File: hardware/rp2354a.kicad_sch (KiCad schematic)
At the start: 31 parts, among them J2 SM03B-SRSS-TB, J3 AM32_1, J4 AM32_2, U4 RP2354A, Y1 ABM8-272-T3

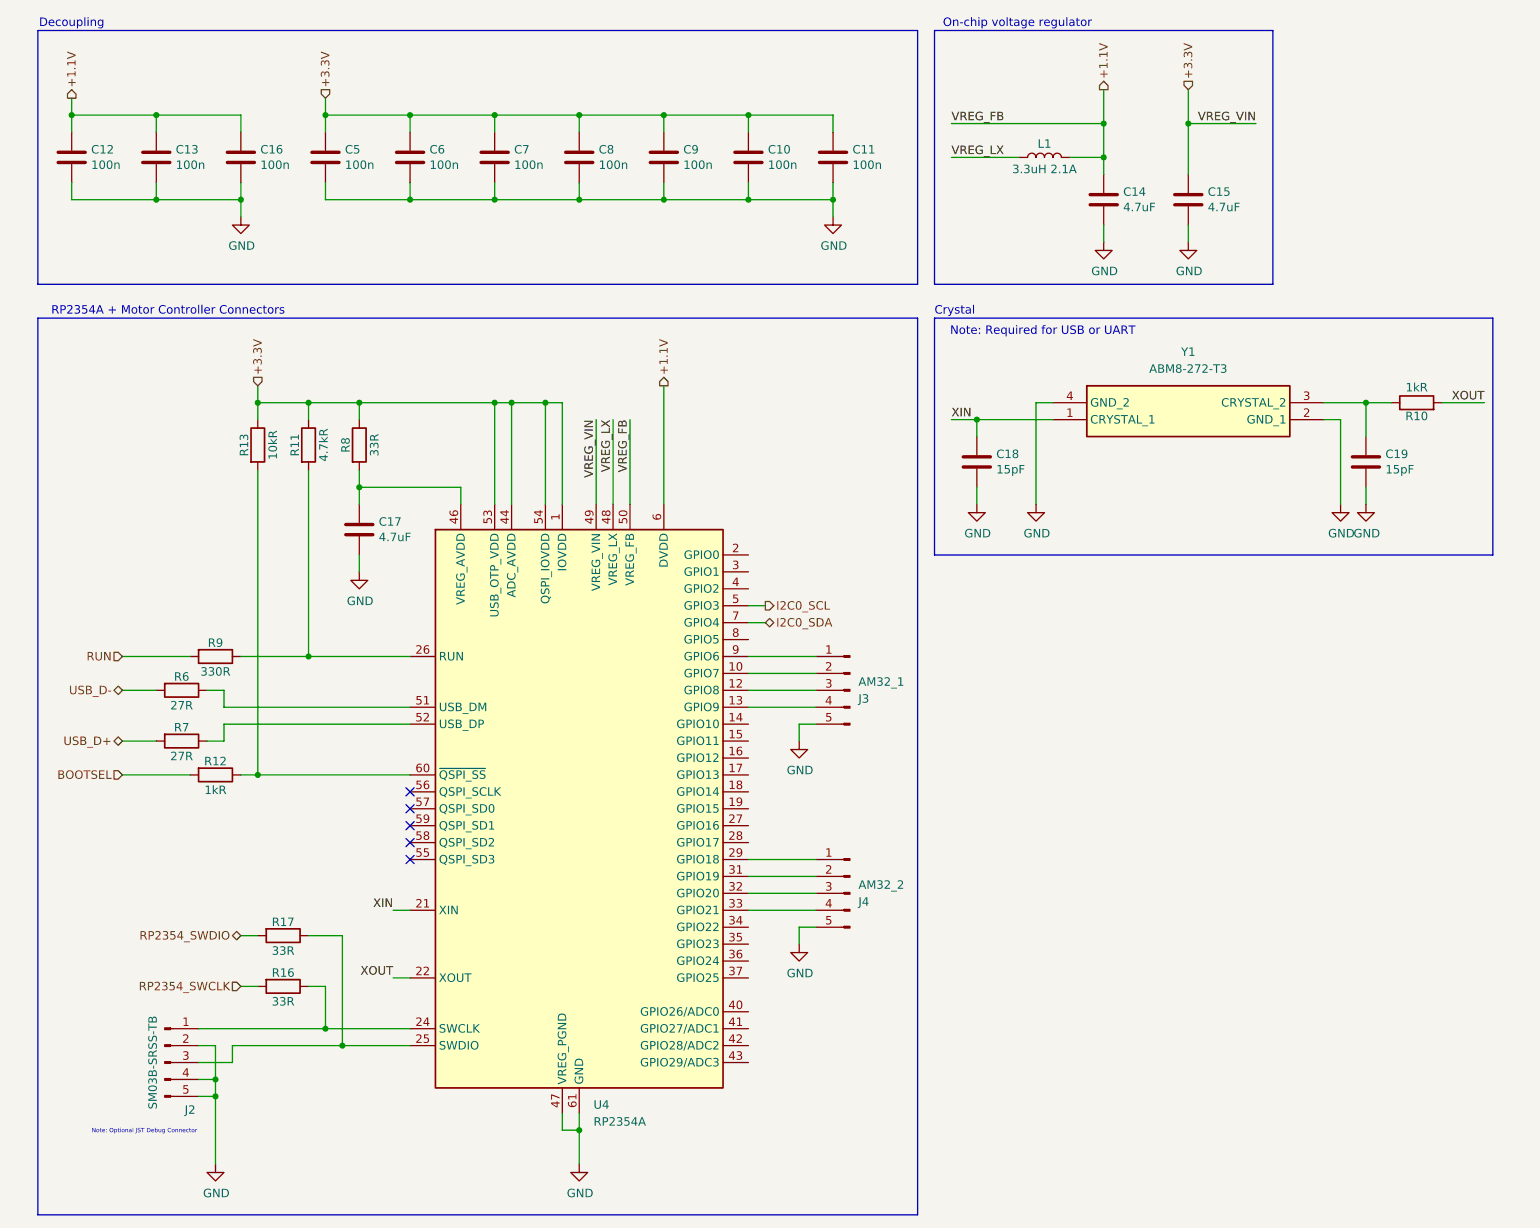
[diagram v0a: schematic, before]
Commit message: Add second camera, magnet load switch and schematic fixes
- Second camera J11 on MIPI1: I2C on ID_SD/ID_SC with 2.2k pull-ups,
  power enable on GPIO14/15 (CAM1_GPIO0/1); both cameras take 3.3 V
  from CM5_3.3V
- Magnet power switch: IC9 output is now +5V_AON, TPS22965 load switch
  IC15 drives +5V, J12 carries +5V_AON / MAG_ON / GND with R29
  pull-down; new TPS22965 symbol library
- Power: 4 A TPSM53604, 8 mOhm input sense resistor, C39/C40 bulk caps,
  F1-F3 battery polyfuses; 5 V raised to 5.115 V (R24 2.43k, 0.5 %
  feedback resistors); 47 uF at the CM5 5 V pins
- BMI270 on SPI and WSEN-PADS on I2C in serial_peripherals.kicad_sch
- Breakout headers J9/J13 with 5 V, 3.3 V and GND
- References renamed U -> IC; net classes for DPHY1, +5V, +5V_AON, +3.3V
- ERC clean (0 errors, 0 warnings); PCB update from the schematic is
  still in progress

Co-Authored-By: Claude Opus 5.5 <noreply@anthropic.com>
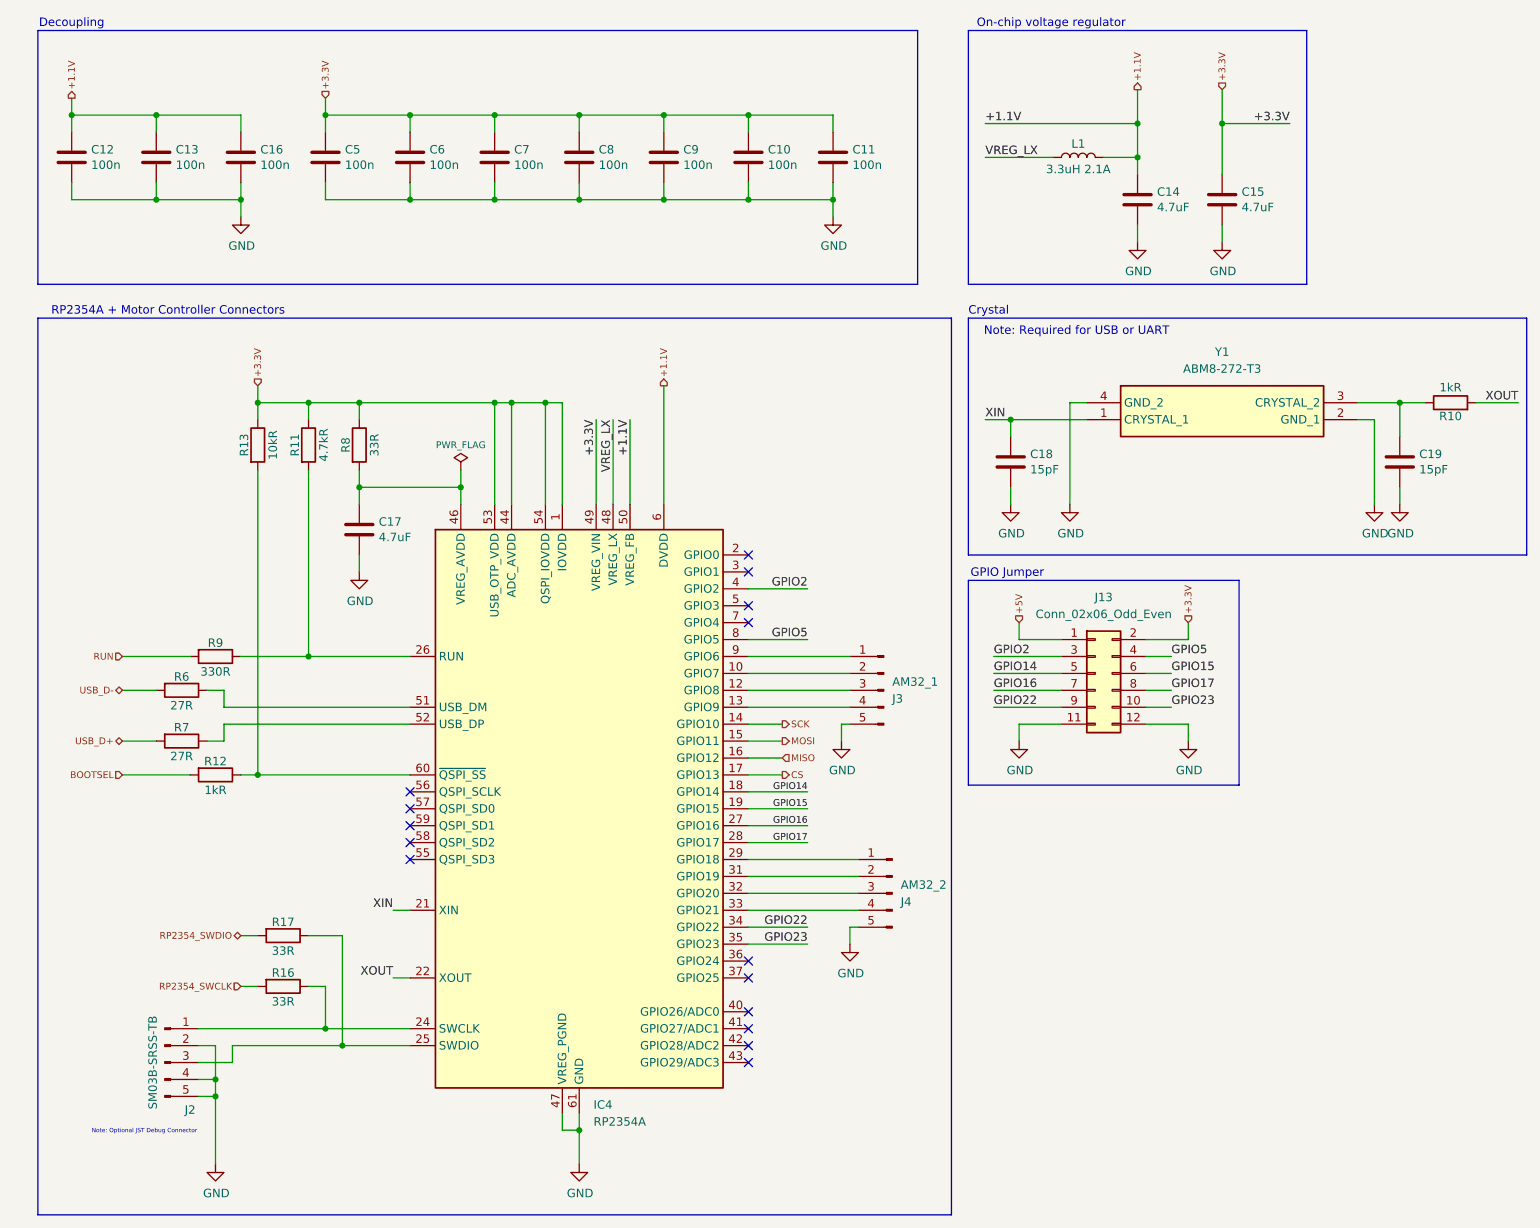
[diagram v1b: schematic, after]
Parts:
- added J13: Conn_02x06_Odd_Even, Connector_PinHeader_1.27mm:PinHeader_2x06_P1.27mm_Vertical, symbol Connector_Generic:Conn_02x06_Odd_Even
- renumbered U4 to IC4
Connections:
- net +3.3V: now also J13.2 (Pin_2)
- net GND: now also J13.11 (Pin_11), J13.12 (Pin_12)
- net SCK: now reaches IC4.14 (GPIO10)
- net MOSI: now reaches IC4.15 (GPIO11)
- net MISO: now reaches IC4.16 (GPIO12)
- net CS: now reaches IC4.17 (GPIO13)
- net GPIO14: now reaches IC4.18 (GPIO14)
- net GPIO14: now also J13.5 (Pin_5)
- net GPIO15: now reaches IC4.19 (GPIO15)
- net GPIO15: now also J13.6 (Pin_6)
- net GPIO16: now reaches IC4.27 (GPIO16)
- net GPIO16: now also J13.7 (Pin_7)
- net GPIO17: now reaches IC4.28 (GPIO17)
- net GPIO17: now also J13.8 (Pin_8)
- net GPIO22: now reaches IC4.34 (GPIO22)
- net GPIO22: now also J13.9 (Pin_9)
- net GPIO23: now reaches IC4.35 (GPIO23)
- net GPIO23: now also J13.10 (Pin_10)
- net GPIO2: now reaches IC4.4 (GPIO2)
- net GPIO2: now also J13.3 (Pin_3)
- net GPIO5: now reaches IC4.8 (GPIO5)
- net GPIO5: now also J13.4 (Pin_4)
- net I2C0_SCL: no longer names the net of IC4.5 (GPIO3)
- net I2C0_SDA: no longer names the net of IC4.7 (GPIO4)
- new net +5V: J13.1 (Pin_1)
- no-connect marks 5 -> 15
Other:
- note added: "GPIO Jumper"
- moved on the sheet: C14, C15, C18, C19, J3, J4, L1, R10, Y1

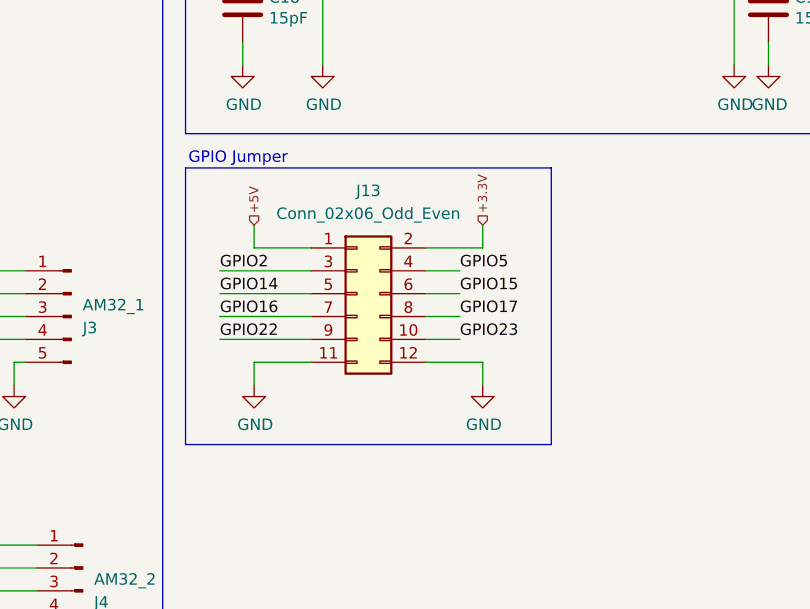
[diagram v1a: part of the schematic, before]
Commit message: Separate the supply pins on breakout headers J9 and J13
Both headers now start with +5V, GND, GND, +3.3V (pins 1-4), so 5 V
and 3.3 V only meet diagonally and each supply pin has GND beside it.
The GPIOs that sat on pins 3/4 moved to the end of each header.

Co-Authored-By: Claude Opus 5.5 <noreply@anthropic.com>
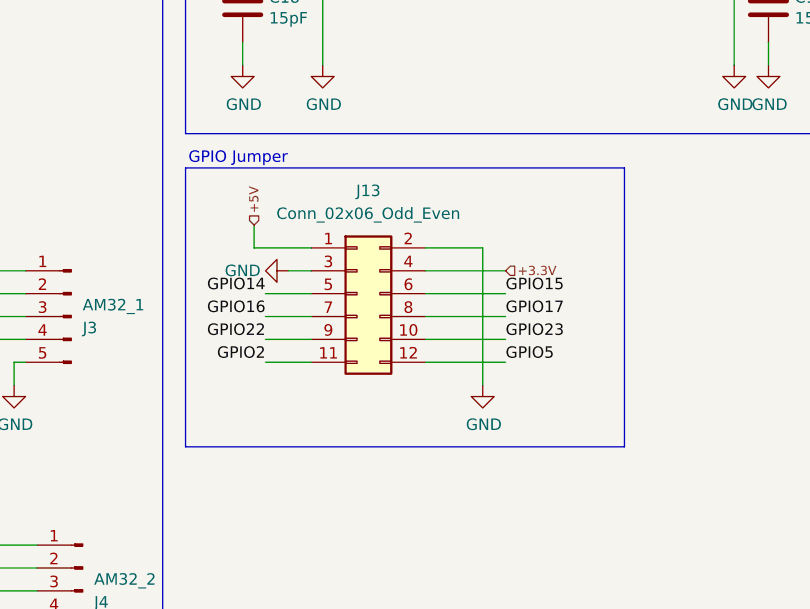
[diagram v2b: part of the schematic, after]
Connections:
- net +3.3V: now also J13.4 (Pin_4); no longer J13.2 (Pin_2)
- net GND: now also J13.2 (Pin_2), J13.3 (Pin_3); no longer J13.11 (Pin_11), J13.12 (Pin_12)
- net GPIO2: now also J13.11 (Pin_11); no longer J13.3 (Pin_3)
- net GPIO5: now also J13.12 (Pin_12); no longer J13.4 (Pin_4)

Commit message: Redo the PCB layout: 70 x 90 mm, power section grouped, one-side reflow
- Second camera connector J11 beside J5 on the top edge.
- SHT45 on a slotted tongue (no pour, no vias, four tracks over a 2.5 mm
  bridge) for thermal decoupling.
- All fine-pitch parts on top; the bottom holds only hand-solderable parts
  (IC5, connectors, 0603+ passives, fuses, electrolytics).
- MagJack, PoE module, charger, 5 V buck and battery connector grouped in
  the bottom half.
- Four M2 mounting holes H1-H4; silkscreen labels for the connectors and
  pin tables for J7, J9 and J13 on the bottom.
- Header pins remapped to simplify routing: J9 (CM5 GPIO), J13 (RP2354A
  GPIO22-29) and J7 (CM5 config); schematic labels updated to match.
- Default clearance 0.1 mm; DRC rules for C20's thermal, top parts under the
  CM5, IC10's land pattern and the edge parts.
- DRC: 0 errors, schematic parity clean; one expected unconnected item
  (CM5 connector-A GND pin 7, tied inside the CM5).

Co-Authored-By: Claude Opus 5.5 <noreply@anthropic.com>
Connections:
- net GPIO22: now also J13.6 (Pin_6); no longer J13.9 (Pin_9)
- net GPIO23: now also J13.11 (Pin_11); no longer J13.10 (Pin_10)
- net GPIO24: now reaches IC4.36 (GPIO24)
- net GPIO24: now also J13.8 (Pin_8)
- net GPIO25: now reaches IC4.37 (GPIO25)
- net GPIO25: now also J13.9 (Pin_9)
- net GPIO26: now reaches IC4.40 (GPIO26/ADC0)
- net GPIO26: now also J13.10 (Pin_10)
- net GPIO27: now reaches IC4.41 (GPIO27/ADC1)
- net GPIO27: now also J13.7 (Pin_7)
- net GPIO28: now reaches IC4.42 (GPIO28/ADC2)
- net GPIO28: now also J13.12 (Pin_12)
- net GPIO29: now reaches IC4.43 (GPIO29/ADC3)
- net GPIO29: now also J13.5 (Pin_5)
- net GPIO14: no longer names the net of IC4.18 (GPIO14)
- net GPIO14: no longer J13.5 (Pin_5)
- net GPIO15: no longer names the net of IC4.19 (GPIO15)
- net GPIO15: no longer J13.6 (Pin_6)
- net GPIO16: no longer names the net of IC4.27 (GPIO16)
- net GPIO16: no longer J13.7 (Pin_7)
- net GPIO17: no longer names the net of IC4.28 (GPIO17)
- net GPIO17: no longer J13.8 (Pin_8)
- net GPIO2: no longer names the net of IC4.4 (GPIO2)
- net GPIO2: no longer J13.11 (Pin_11)
- net GPIO5: no longer names the net of IC4.8 (GPIO5)
- net GPIO5: no longer J13.12 (Pin_12)

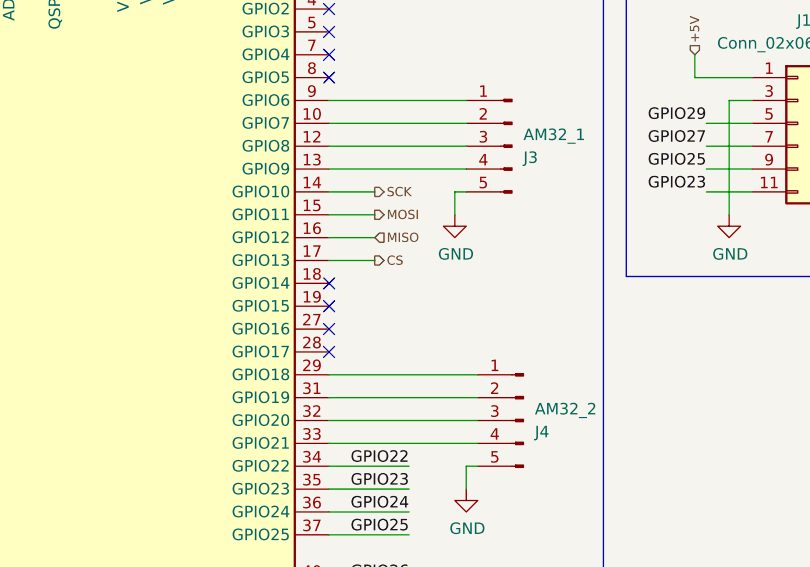
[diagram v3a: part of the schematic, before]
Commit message: Add switchable ESC power, vertical camera connectors and 3.3 V decoupling
- ESC power switch on the root sheet:
  - Battery input J6 changes to XT60PW-M. New XT60PW-F J14 carries switched
    power to both ESCs.
  - Q3 (onsemi NTMFS5C404NLT1G, 40 V, 0.67 mOhm) is driven by the photovoltaic
    driver IC16 (Vishay VOM1271T) from RP2354A GPIO14 (ESC_PWR_EN) via R31.
  - Soft start C46/D6/R32 keeps Q3 in its SOA while the ESC capacitors charge.
    D7 clamps the gate when the battery is unplugged or the thrusters windmill.
  - Static switch with no current limit: the battery BMS protects. Firmware
    timing rules are in the schematic note and the README.
- Camera connectors J5/J11 are now Molex 501951-2230 (vertical, flip lock).
  The footprint numbers pads n = Molex circuit 23-n so a standard Pi 22-pin
  cable lands GND on pin 1, as on the CM5 IO Board.
- Decoupling: 10 uF + 100 nF at the CM5 3.3 V output, 10 uF at each camera
  supply pin.
- Polyfuses F1-F3 removed; the battery feeds the charger path directly.
- New libraries VOM1271T, NTMFS5C404NL, Molex and Vishay, with 3D models.
- PCB updated from the schematic. The layout will be redone.

Co-Authored-By: Claude Opus 5.5 <noreply@anthropic.com>
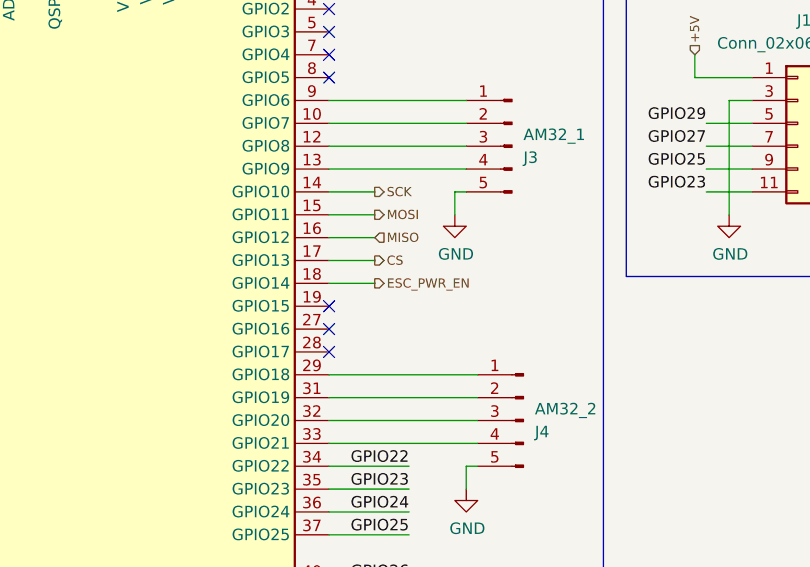
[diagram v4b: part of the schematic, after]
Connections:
- net ESC_PWR_EN: now reaches IC4.18 (GPIO14)
- no-connect marks 15 -> 14
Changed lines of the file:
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@@
 	)
 	(no_connect
+		(at 121.92 139.7)
+	)
+	(no_connect
+		(at 121.92 109.22)
+	)
+	(no_connect
 		(at 121.92 96.52)
 	)
 	(no_connect
+		(at 121.92 134.62)
+	)
+	(no_connect
 		(at 71.12 142.24)
 	)
 	(no_connect
+		(at 121.92 137.16)
+	)
+	(no_connect
 		(at 121.92 106.68)
 	)
@@
 	)
 	(no_connect
+		(at 121.92 101.6)
+	)
+	(no_connect
 		(at 71.12 137.16)
 	)
@@
 	(wire
 		(pts
+			(xy 121.92 132.08) (xy 127 132.08)
+		)
+		(stroke
+			(width 0)
+			(type solid)
+		)
+	)
+	(wire
+		(pts
 			(xy 121.92 147.32) (xy 138.43 147.32)
 		)
@@
 	(wire
 		(pts
+			(xy 121.92 160.02) (xy 130.81 160.02)
+		)
+		(stroke
+			(width 0)
+			(type default)
+		)
+	)
+	(wire
+		(pts
 			(xy 121.92 154.94) (xy 130.81 154.94)
 		)
@@
 	(wire
 		(pts
+			(xy 121.92 167.64) (xy 130.81 167.64)
+		)
+		(stroke
+			(width 0)
+			(type default)
+		)
+	)
+	(wire
+		(pts
 			(xy 83.82 30.48) (xy 96.52 30.48)
 		)
@@
 	(wire
 		(pts
+			(xy 121.92 165.1) (xy 130.81 165.1)
+		)
+		(stroke
+			(width 0)
+			(type default)
+		)
+	)
+	(wire
+		(pts
 			(xy 193.04 46.99) (xy 193.04 49.53)
 		)
@@
 	(wire
 		(pts
+			(xy 121.92 170.18) (xy 130.81 170.18)
+		)
+		(stroke
+			(width 0)
+			(type default)
+		)
+	)
+	(wire
+		(pts
 			(xy 180.34 36.83) (xy 180.34 39.37)
 		)
@@
 	(wire
 		(pts
+			(xy 121.92 157.48) (xy 130.81 157.48)
+		)
+		(stroke
+			(width 0)
+			(type default)
+		)
+	)
+	(wire
+		(pts
 			(xy 181.61 114.3) (xy 190.5 114.3)
 		)
@@
 	(wire
 		(pts
+			(xy 121.92 172.72) (xy 130.81 172.72)
+		)
+		(stroke
+			(width 0)
+			(type default)
+		)
+	)
+	(wire
+		(pts
 			(xy 93.98 180.34) (xy 93.98 182.88)
 		)
@@
 	)
 	(label "GPIO24"
+		(at 130.81 157.48 180)
+		(effects
+			(font
+				(size 1.27 1.27)
+			)
+			(justify right bottom)
+		)
+	)
+	(label "GPIO24"
 		(at 190.5 116.84 0)
 		(effects
@@
 		)
 	)
+	(label "GPIO25"
+		(at 130.81 160.02 180)
+		(effects
+			(font
+				(size 1.27 1.27)
+			)
+			(justify right bottom)
+		)
+	)
 	(label "GPIO22"
 		(at 190.5 114.3 0)
@@
 		)
 	)
+	(label "GPIO29"
+		(at 130.81 172.72 180)
+		(effects
+			(font
+				(size 1.27 1.27)
+			)
+			(justify right bottom)
+		)
+	)
 	(label "GPIO26"
 		(at 190.5 119.38 0)
@@
 		)
 	)
+	(label "GPIO28"
+		(at 130.81 170.18 180)
+		(effects
+			(font
+				(size 1.27 1.27)
+			)
+			(justify right bottom)
+		)
+	)
 	(label "GPIO25"
 		(at 163.83 119.38 180)
@@
 		)
 	)
+	(label "GPIO27"
+		(at 130.81 167.64 180)
+		(effects
+			(font
+				(size 1.27 1.27)
+			)
+			(justify right bottom)
+		)
+	)
 	(label "GPIO23"
 		(at 130.81 154.94 180)
@@
 		)
 	)
+	(label "GPIO26"
+		(at 130.81 165.1 180)
+		(effects
+			(font
+				(size 1.27 1.27)
+			)
+			(justify right bottom)
+		)
+	)
 	(label "GPIO28"
 		(at 190.5 121.92 0)
@@
 		)
 	)
+	(hierarchical_label "ESC_PWR_EN"
+		(shape output)
+		(at 127 132.08 0)
+		(effects
+			(font
+				(size 1.016 1.016)
+			)
+			(justify left)
+		)
+	)
 	(hierarchical_label "+5V"
 		(shape input)
@@
 		)
 	)
-	(no_connect
-		(at 121.92 101.6)
-	)
-	(no_connect
-		(at 121.92 109.22)
-	)
-	(no_connect
-		(at 121.92 132.08)
-	)
-	(no_connect
-		(at 121.92 134.62)
-	)
-	(no_connect
-		(at 121.92 137.16)
-	)
-	(no_connect
-		(at 121.92 139.7)
-	)
-	(wire
-		(pts
-			(xy 121.92 157.48) (xy 130.81 157.48)
-		)
-		(stroke
-			(width 0)
-			(type default)
-		)
-	)
-	(label "GPIO24"
-		(at 130.81 157.48 180)
-		(effects
-			(font
-				(size 1.27 1.27)
-			)
-			(justify right bottom)
-		)
-	)
-	(wire
-		(pts
-			(xy 121.92 160.02) (xy 130.81 160.02)
-		)
-		(stroke
-			(width 0)
-			(type default)
-		)
-	)
-	(label "GPIO25"
-		(at 130.81 160.02 180)
-		(effects
-			(font
-				(size 1.27 1.27)
-			)
-			(justify right bottom)
-		)
-	)
-	(wire
-		(pts
-			(xy 121.92 165.1) (xy 130.81 165.1)
-		)
-		(stroke
-			(width 0)
-			(type default)
-		)
-	)
-	(label "GPIO26"
-		(at 130.81 165.1 180)
-		(effects
-			(font
-				(size 1.27 1.27)
-			)
-			(justify right bottom)
-		)
-	)
-	(wire
-		(pts
-			(xy 121.92 167.64) (xy 130.81 167.64)
-		)
-		(stroke
-			(width 0)
-			(type default)
-		)
-	)
-	(label "GPIO27"
-		(at 130.81 167.64 180)
-		(effects
-			(font
-				(size 1.27 1.27)
-			)
-			(justify right bottom)
-		)
-	)
-	(wire
-		(pts
-			(xy 121.92 170.18) (xy 130.81 170.18)
-		)
-		(stroke
-			(width 0)
-			(type default)
-		)
-	)
-	(label "GPIO28"
-		(at 130.81 170.18 180)
-		(effects
-			(font
-				(size 1.27 1.27)
-			)
-			(justify right bottom)
-		)
-	)
-	(wire
-		(pts
-			(xy 121.92 172.72) (xy 130.81 172.72)
-		)
-		(stroke
-			(width 0)
-			(type default)
-		)
-	)
-	(label "GPIO29"
-		(at 130.81 172.72 180)
-		(effects
-			(font
-				(size 1.27 1.27)
-			)
-			(justify right bottom)
-		)
-	)
